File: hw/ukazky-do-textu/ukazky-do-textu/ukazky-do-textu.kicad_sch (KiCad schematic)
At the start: 7 parts, among them J1 Konektor

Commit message: schemata a 3d modely pro text
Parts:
- removed D1, D2: 1N914, Diode_THT:D_DO-35_SOD27_P7.62mm_Horizontal, symbol Diode:1N914
- removed D3: D_Zener, symbol Device:D_Zener
- removed F1, F2: Polyfuse, symbol Device:Polyfuse
- removed J1: Konektor, symbol Connector:Conn_01x03_Pin
- added C1: 2x10uF, Capacitor_SMD:C_1210_3225Metric_Pad1.33x2.70mm_HandSolder, symbol Device:C
- added C2: 6.8nF, Capacitor_SMD:C_0805_2012Metric_Pad1.18x1.45mm_HandSolder, symbol Device:C
- added C3, C4, C5: 100nF, Capacitor_SMD:C_0805_2012Metric_Pad1.18x1.45mm_HandSolder, symbol Device:C
- added C6: 3x22uF, Capacitor_SMD:C_0805_2012Metric_Pad1.18x1.45mm_HandSolder, symbol Device:C
- added D1: RB501SM, Diode_SMD:D_SOD-523, symbol Device:D
- added L1: 10uH, Inductor_SMD:L_Changjiang_FNR6045S, symbol Device:L
- added R2: 47k, Resistor_SMD:R_0805_2012Metric_Pad1.20x1.40mm_HandSolder, symbol Device:R
- added R3: 140k, Resistor_SMD:R_0805_2012Metric_Pad1.20x1.40mm_HandSolder, symbol Device:R
- added R4: 10k, Resistor_SMD:R_0805_2012Metric_Pad1.20x1.40mm_HandSolder, symbol Device:R
- added R5: 100k, Resistor_SMD:R_0805_2012Metric_Pad1.20x1.40mm_HandSolder, symbol Device:R
- added R6: 10m, Resistor_SMD:R_0815_2038Metric_Pad1.20x4.05mm_HandSolder, symbol Device:R
- added U1: AP63356Q, Library:V-DFN3020-13, symbol buck-lib:AP63356Q
- added U2: INA180A4, Package_TO_SOT_SMD:SOT-23-5, symbol Amplifier_Current:INA180A4
- R1: value R -> 100k; footprint (none) -> Resistor_SMD:R_0805_2012Metric_Pad1.20x1.40mm_HandSolder
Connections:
- net GND: now also R1.2, C1.2, C2.1, C4.1, C5.2, C6.2, R4.2, U1.8 (GND), U2.2 (GND)
- net DATA_PIN renamed RA2
- net RA2: now also U1.2 (EN)
- new net: C6.1, L1.1, R3.1, R6.2, U2.3 (+)
- new net: C3.2, L1.2, U1.9 (SW)
- new net: R3.2, R4.1, R5.1, U1.3 (FB)
- new net: D1.1 (K), R5.2
- new net: C4.2, R2.1, U1.4 (COMP)
- new net: C2.2, R2.2
- new net: C3.1, U1.6 (BST)
- new net 24V: C1.1, U1.1 (VIN)
- new net LED_OUT_0: R6.1, U2.4 (-)
- new net RA3: D1.2 (A)
- new net RA4: U1.5 (PG)
- new net RB1: U2.1
- new net VDD: C5.1, U2.5 (V+)
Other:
- note added: "I."
- note added: "II."
- note removed: "1"

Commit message: text - revize napsaneho, schema lm
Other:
- added sheet Untitled Sheet (main-b-simply.kicad_sch)
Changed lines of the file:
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@@
+    )
+  )
+  (sheet (at 210.82 64.77) (size 38.1 27.94) (fields_autoplaced)
+    (stroke (width 0.1524) (type solid))
+    (fill (color 0 0 0 0.0000))
+    (property "Sheetname" "Untitled Sheet" (at 210.82 64.0584 0)
+      (effects (font (size 1.27 1.27)) (justify left bottom))
+    )
+    (property "Sheetfile" "main-b-simply.kicad_sch" (at 210.82 93.2946 0)
+      (effects (font (size 1.27 1.27)) (justify left top))
+    )
+    (instances
+      (project "ukazky-do-textu"
+        (path "/5ea9602d-a3cc-4e11-96b1-d08bdd6d2ed5" (page "2"))
+      )
     )
   )

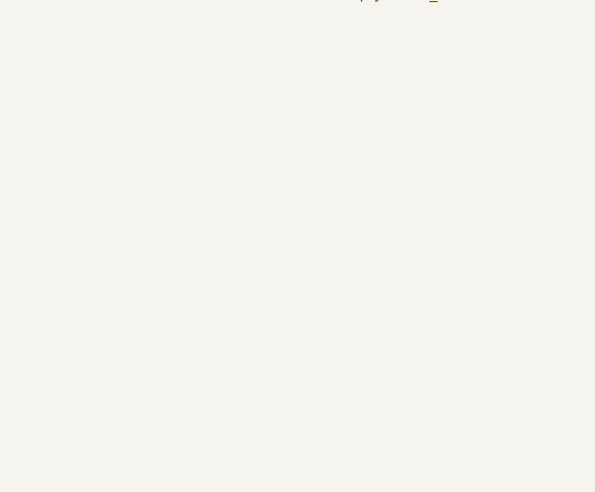
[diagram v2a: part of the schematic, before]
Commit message: text - 230v, wl sensor
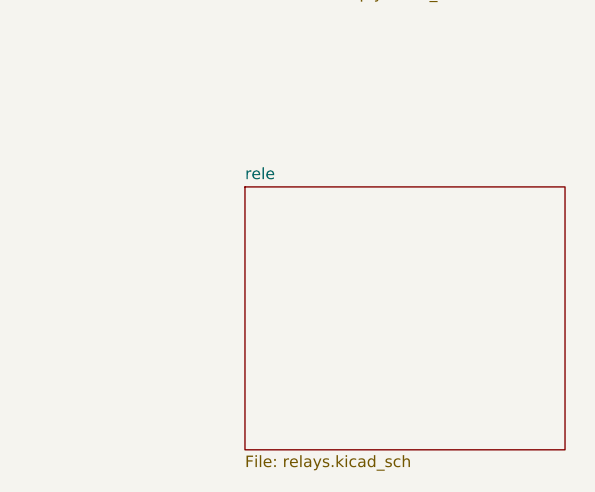
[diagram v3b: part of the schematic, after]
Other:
- added sheet rele (relays.kicad_sch)
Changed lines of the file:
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@@
+    )
+  )
+  (sheet (at 212.09 115.57) (size 35.56 29.21) (fields_autoplaced)
+    (stroke (width 0.1524) (type solid))
+    (fill (color 0 0 0 0.0000))
+    (property "Sheetname" "rele" (at 212.09 114.8584 0)
+      (effects (font (size 1.27 1.27)) (justify left bottom))
+    )
+    (property "Sheetfile" "relays.kicad_sch" (at 212.09 145.3646 0)
+      (effects (font (size 1.27 1.27)) (justify left top))
+    )
+    (instances
+      (project "ukazky-do-textu"
+        (path "/5ea9602d-a3cc-4e11-96b1-d08bdd6d2ed5" (page "3"))
+      )
     )
   )
